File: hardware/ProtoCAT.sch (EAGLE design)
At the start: 53 parts, among them U1 ARDUINO

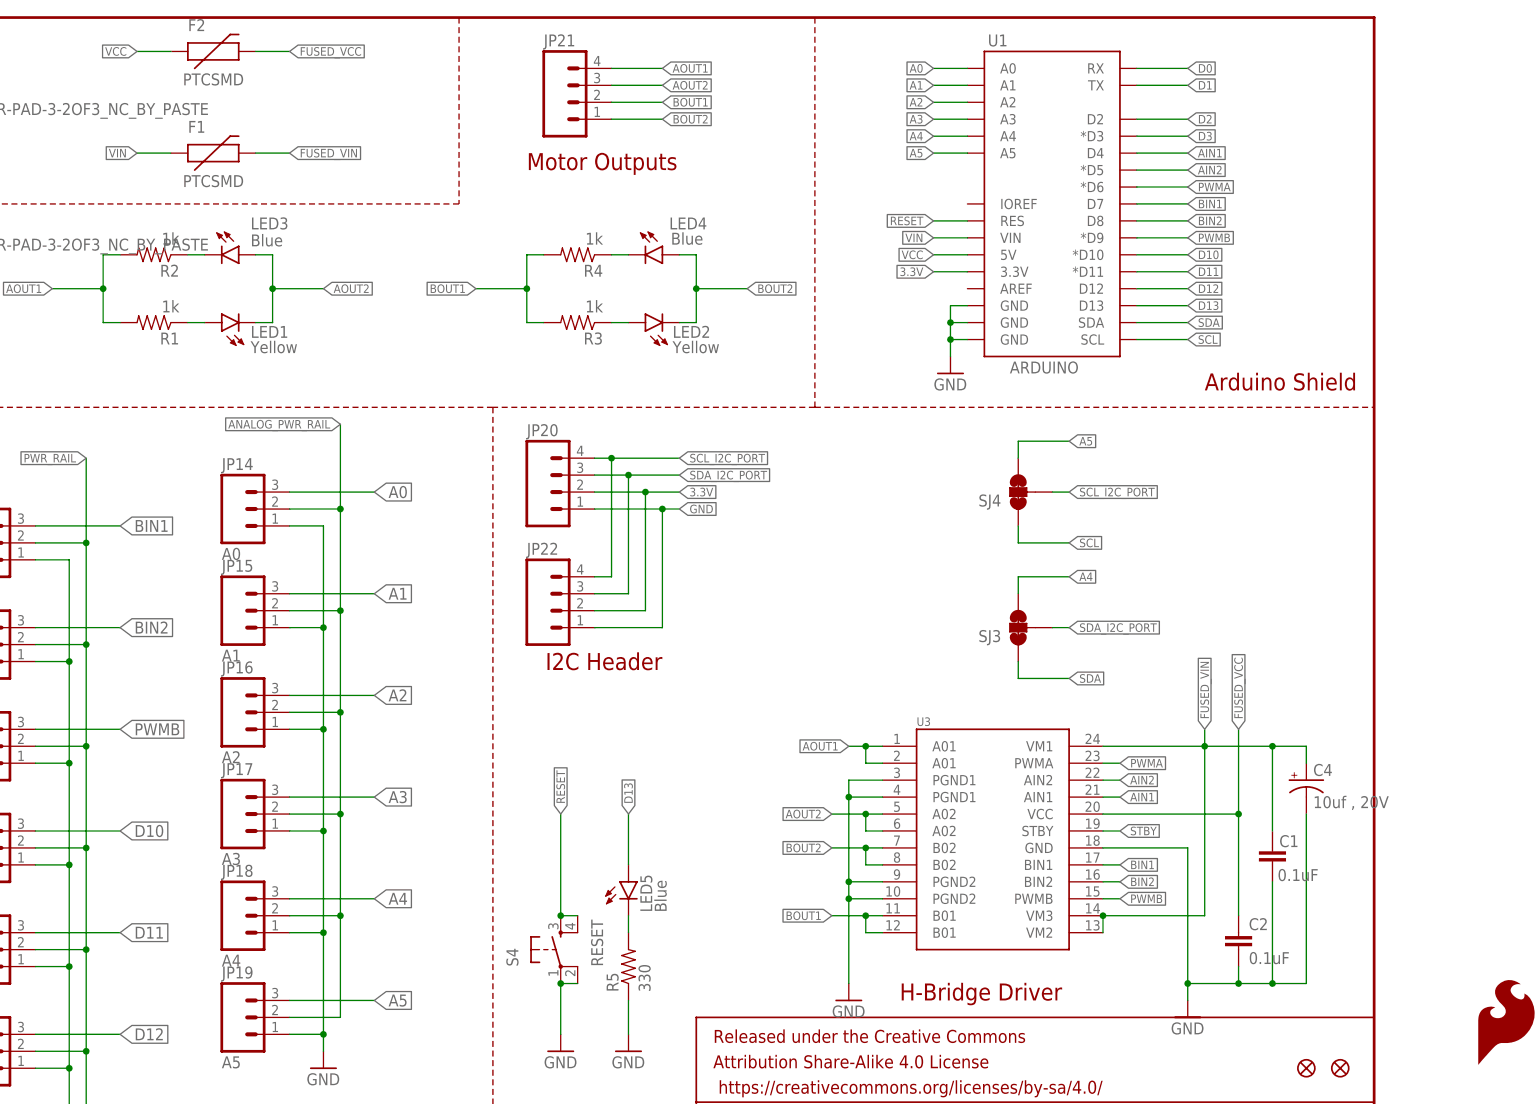
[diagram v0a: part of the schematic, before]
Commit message: Moved 4 pin SMD headers to Motor Driver
Tied STDBY pin on motor driver to Vcc, added 4 pin SMD header to motor
Driver output, and changed 3-pin headers to locking headers
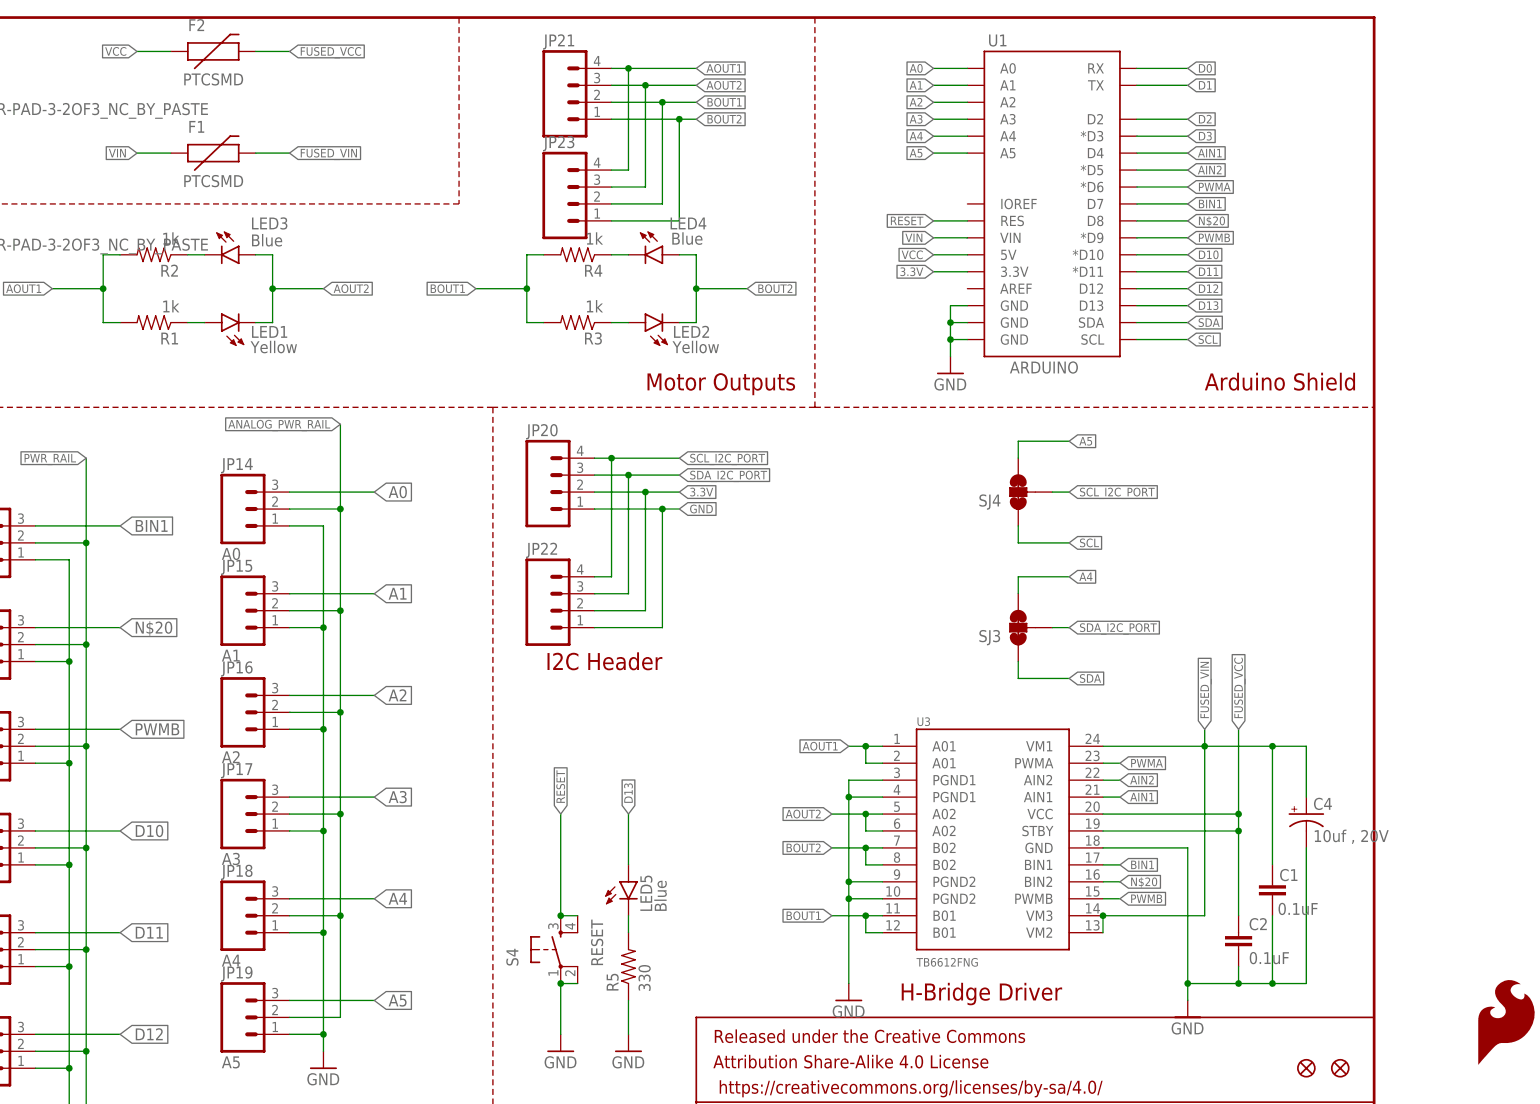
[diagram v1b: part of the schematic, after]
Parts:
- added JP23: (no value), SparkFun-Connectors:M04SMD_STRAIGHT_COMBO
- FID1, FID2: value FIDUCIALUFIDUCIAL -> FIDUCIAL1X2; device SparkFun-Aesthetics:FIDUCIALUFIDUCIAL -> SparkFun-Aesthetics:FIDUCIAL1X2
- JP0, JP1, JP10, JP11, JP12, JP13, JP14, JP15, JP16, JP17, JP18, JP19, JP2, JP3, JP4, JP5, JP6, JP7, JP8, JP9: device SparkFun-Connectors:M03PTH -> SparkFun-Connectors:M03LOCK
- U3: value (none) -> TB6612FNG; device SparkFun-PowerIC:TB6621FNG -> SparkFun-PowerIC:TB6612FNG
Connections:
- net BIN2 renamed N$20
- removed net STBY: U3.STBY
- net AOUT1: now also JP23.4
- net AOUT2: now also JP23.3
- net BOUT1: now also JP23.2
- net BOUT2: now also JP23.1
- net FUSED_VCC: now also U3.STBY
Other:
- moved on the sheet: C1, C4

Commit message: Initial Commit
Updated / Changed ProtoCAT to include an XBee header
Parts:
- removed JP20: (no value), SparkFun-Connectors:M04SMD_STRAIGHT_COMBO
- added LED7: Red, SparkFun-LED:LED-RED0603
- added LED8, LED9: Green, SparkFun-LED:LED-GREEN0603
- added MOD1: XBEE-1XBEE-1_LOCK, SparkFun-RF:XBEE-1XBEE-1_LOCK
- added Q1, Q2: MOSFET-NCHANNELSMD, SparkFun-DiscreteSemi:MOSFET-NCHANNELSMD
- added R10, R12, R13, R6, R7, R8, R9: 1k, SparkFun-Resistors:1KOHM1/10W1%(0603)
- added S3: DPDT, SparkFun-Electromechanical:SWITCH-DPDTAYZ0202
- FRAME1: value FRAME-LETTER -> FRAME-LEDGER; device SparkFun-Aesthetics:FRAME-LETTER -> SparkFun-Aesthetics:FRAME-LEDGER
- JP22: device SparkFun-Connectors:M04PTH -> SparkFun-Connectors:M04SMD_STRAIGHT_COMBO
- JP23: device SparkFun-Connectors:M04SMD_STRAIGHT_COMBO -> SparkFun-Connectors:M04PTH
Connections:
- net N$20 renamed BIN2
- removed net A0: JP14.3, U1.A0
- removed net A1: JP15.3, U1.A1
- removed net D0: JP0.3, U1.RX
- removed net D1: JP1.3, U1.TX
- new net 5V: R10.2, R13.2
- new net A0/SW_RXI: JP14.3, S3.6, U1.A0
- new net A1/SW_TXO: JP15.3, S3.3, U1.A1
- new net D0_RXI: JP0.3, S3.4, U1.RX
- new net D1_TXO: JP1.3, S3.1, U1.TX
- new net DIN: LED8.C, MOD1.DIN, Q1.S, R9.1
- new net DOUT: LED7.C, MOD1.DOUT, Q2.S, R12.1
- new net N$22: LED7.A, R6.2
- new net N$43: LED8.A, R7.2
- new net N$44: LED9.A, R8.1
- new net RSSI: MOD1.RSSI, R8.2
- new net XBEE_RESET: MOD1.RESET
- new net XBEE_RXI: Q2.D, R13.1, S3.2
- new net XBEE_TXO: Q1.D, R10.1, S3.5
- net 3.3V: now also JP23.2, MOD1.VDD, Q1.G, Q2.G, R12.2, R6.1, R7.1, R9.2; no longer JP20.2, JP22.2
- net AOUT1: now also JP22.4; no longer JP23.4
- net AOUT2: now also JP22.3; no longer JP23.3
- net BOUT1: now also JP22.2; no longer JP23.2
- net BOUT2: now also JP22.1; no longer JP23.1
- net GND: now also JP23.1, LED9.C, MOD1.GND; no longer JP20.1, JP22.1
- net SCL_I2C_PORT: now also JP23.4; no longer JP20.4, JP22.4
- net SDA_I2C_PORT: now also JP23.3; no longer JP20.3, JP22.3
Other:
- note added: "3 Pin Header Field"
- note added: "v11"
- note removed: "v01"
- moved on the sheet: F1, F2, JP0, JP1, JP10, JP11, JP12, JP13, JP14, JP15, JP16, JP17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
